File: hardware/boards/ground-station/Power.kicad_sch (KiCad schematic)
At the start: 19 parts, among them J1 USB_A, J2 Barrel_Jack, U3 TPS564242DRLR

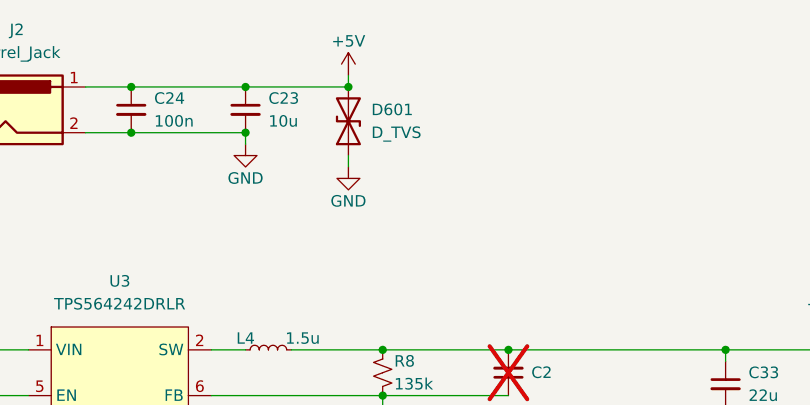
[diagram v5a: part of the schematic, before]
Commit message: Added a couple more footprints, changed TVS diode to uni-directional
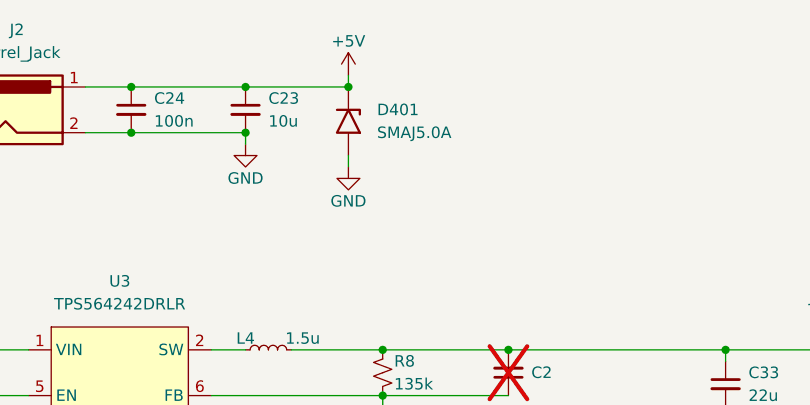
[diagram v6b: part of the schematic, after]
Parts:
- removed D601: D_TVS, symbol Device:D_TVS
- added D401: SMAJ5.0A, Diode_SMD:D_SMA, symbol Diode:SMAJ5.0A
- J1: footprint (none) -> Connector_USB:USB_A_Molex_67643_Horizontal; Part No USB-A-S-RA -> Molex 67643
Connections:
- net +5V: now also D401.1 (A1)
- net GND: now also D401.2 (A2)
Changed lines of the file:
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@@
   (junction (at 143.51 63.5) (diameter 0) (color 0 0 0 0)
   )
+  (junction (at 171.45 87.63) (diameter 0) (color 0 0 0 0)
+  )
+  (junction (at 209.55 87.63) (diameter 0) (color 0 0 0 0)
+  )
+  (junction (at 125.73 87.63) (diameter 0) (color 0 0 0 0)
+  )
+  (junction (at 143.51 58.42) (diameter 0) (color 0 0 0 0)
+  )
+  (junction (at 154.94 101.6) (diameter 0) (color 0 0 0 0)
+  )
+  (junction (at 158.75 135.89) (diameter 0) (color 0 0 0 0)
+  )
+  (junction (at 156.21 58.42) (diameter 0) (color 0 0 0 0)
+  )
+  (junction (at 88.9 87.63) (diameter 0) (color 0 0 0 0)
+  )
+  (junction (at 110.49 87.63) (diameter 0) (color 0 0 0 0)
+  )
+  (junction (at 220.98 87.63) (diameter 0) (color 0 0 0 0)
+  )
+  (junction (at 185.42 87.63) (diameter 0) (color 0 0 0 0)
+  )
+  (junction (at 171.45 92.71) (diameter 0) (color 0 0 0 0)
+  )
+  (junction (at 99.06 87.63) (diameter 0) (color 0 0 0 0)
+  )
   (junction (at 167.64 58.42) (diameter 0) (color 0 0 0 0)
-  )
-  (junction (at 171.45 87.63) (diameter 0) (color 0 0 0 0)
-  )
-  (junction (at 209.55 87.63) (diameter 0) (color 0 0 0 0)
-  )
-  (junction (at 125.73 87.63) (diameter 0) (color 0 0 0 0)
-  )
-  (junction (at 143.51 58.42) (diameter 0) (color 0 0 0 0)
-  )
-  (junction (at 154.94 101.6) (diameter 0) (color 0 0 0 0)
-  )
-  (junction (at 158.75 135.89) (diameter 0) (color 0 0 0 0)
-  )
-  (junction (at 156.21 58.42) (diameter 0) (color 0 0 0 0)
-  )
-  (junction (at 88.9 87.63) (diameter 0) (color 0 0 0 0)
-  )
-  (junction (at 110.49 87.63) (diameter 0) (color 0 0 0 0)
-  )
-  (junction (at 220.98 87.63) (diameter 0) (color 0 0 0 0)
-  )
-  (junction (at 185.42 87.63) (diameter 0) (color 0 0 0 0)
-  )
-  (junction (at 171.45 92.71) (diameter 0) (color 0 0 0 0)
-  )
-  (junction (at 99.06 87.63) (diameter 0) (color 0 0 0 0)
   )
   (no_connect (at 148.59 143.51))
@@
     )
   )
+  (symbol (lib_id "Diode:SMAJ5.0A") (at 167.64 62.23 270) (unit 1)
+    (in_bom yes) (on_board yes) (dnp no) (fields_autoplaced)
+    (property "Reference" "D401" (at 170.815 60.96 90)
+      (effects (font (size 1.27 1.27)) (justify left))
+    )
+    (property "Value" "SMAJ5.0A" (at 170.815 63.5 90)
+      (effects (font (size 1.27 1.27)) (justify left))
+    )
+    (property "Footprint" "Diode_SMD:D_SMA" (at 162.56 62.23 0)
+      (effects (font (size 1.27 1.27)) hide)
+    )
+    (property "Datasheet" "https://www.littelfuse.com/media?resourcetype=datasheets&itemid=75e32973-b177-4ee3-a0ff-cedaf1abdb93&filename=smaj-datasheet" (at 167.64 60.96 0)
+      (effects (font (size 1.27 1.27)) hide)
+    )
+    (pin "1")
+    (pin "2")
+    (instances
+      (project "ground-station"
+        (path "/ce329892-de08-4d39-b253-15f3aaf1c085/448ef7a9-bc5a-4b03-856d-4da8b62bdbd1"
+          (reference "D401") (unit 1)
+        )
+      )
+    )
+  )
   (symbol (lib_id "Connector:Barrel_Jack") (at 130.81 60.96 0) (unit 1)
     (in_bom yes) (on_board yes) (dnp no) (fields_autoplaced)
@@
       (effects (font (size 1.27 1.27)))
     )
-    (property "Footprint" "" (at 144.78 142.24 0)
-      (effects (font (size 1.27 1.27)) hide)
-    )
-    (property "Datasheet" "https://app.adam-tech.com/products/download/data_sheet/195865/usb-a-s-ra-data-sheet.pdf" (at 144.78 142.24 0)
-      (effects (font (size 1.27 1.27)) hide)
-    )
-    (property "Part No" "USB-A-S-RA" (at 140.97 140.97 0)
+    (property "Footprint" "Connector_USB:USB_A_Molex_67643_Horizontal" (at 144.78 142.24 0)
+      (effects (font (size 1.27 1.27)) hide)
+    )
+    (property "Datasheet" "https://tools.molex.com/pdm_docs/sd/676430910_sd.pdf" (at 144.78 142.24 0)
+      (effects (font (size 1.27 1.27)) hide)
+    )
+    (property "Part No" "Molex 67643" (at 140.97 140.97 0)
       (effects (font (size 1.27 1.27)) hide)
     )
@@
         )
       )
-    )
-  )
-  (symbol (lib_id "Device:D_TVS") (at 167.64 62.23 90) (unit 1)
-    (in_bom yes) (on_board yes) (dnp no) (fields_autoplaced)
-    (property "Reference" "D601" (at 170.18 60.96 90)
-      (effects (font (size 1.27 1.27)) (justify right))
-    )
-    (property "Value" "D_TVS" (at 170.18 63.5 90)
-      (effects (font (size 1.27 1.27)) (justify right))
-    )
-    (property "Footprint" "" (at 167.64 62.23 0)
-      (effects (font (size 1.27 1.27)) hide)
-    )
-    (property "Datasheet" "~" (at 167.64 62.23 0)
-      (effects (font (size 1.27 1.27)) hide)
-    )
-    (pin "1")
-    (pin "2")
-    (instances
-      (project "ground-station"
-        (path "/ce329892-de08-4d39-b253-15f3aaf1c085/448ef7a9-bc5a-4b03-856d-4da8b62bdbd1"
-          (reference "D601") (unit 1)
-        )
-      )

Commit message: Did initial layout. Still need to connect everything together
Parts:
- J2: footprint (none) -> capstone:PJ-037A; Part No (none) -> PJ-037A
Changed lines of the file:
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@@
       (effects (font (size 1.27 1.27)))
     )
-    (property "Footprint" "" (at 132.08 61.976 0)
+    (property "Footprint" "capstone:PJ-037A" (at 132.08 61.976 0)
       (effects (font (size 1.27 1.27)) hide)
     )
-    (property "Datasheet" "~" (at 132.08 61.976 0)
+    (property "Datasheet" "https://www.cuidevices.com/product/resource/pj-037a.pdf" (at 132.08 61.976 0)
       (effects (font (size 1.27 1.27)) hide)
     )
+    (property "Part No" "PJ-037A" (at 130.81 60.96 0)
+      (effects (font (size 1.27 1.27)) hide)
+    )
